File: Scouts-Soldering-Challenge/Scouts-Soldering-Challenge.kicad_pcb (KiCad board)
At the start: 2 copper layers, 76.2 x 94 mm, 14 parts, among them SW1 SW_Push

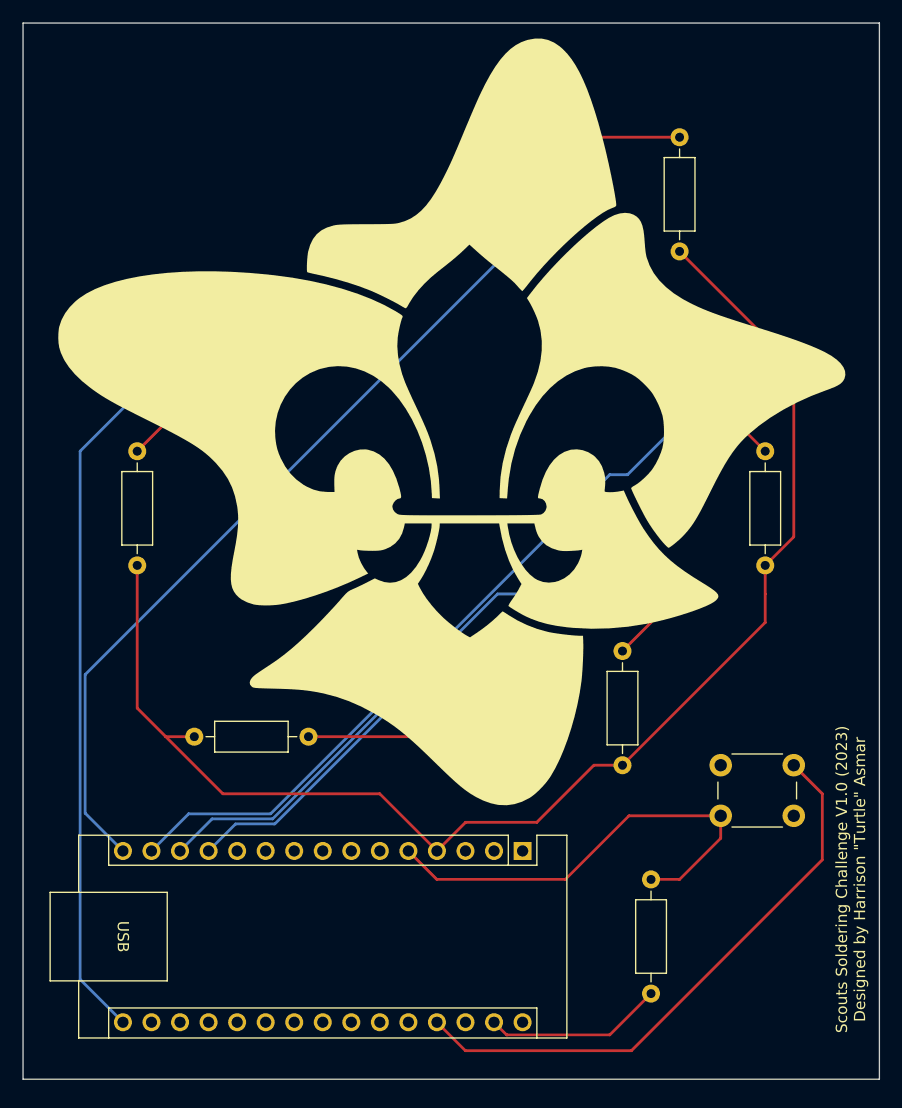
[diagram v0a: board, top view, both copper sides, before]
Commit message: Updated some trace routes
Minor changes, still functionally the same
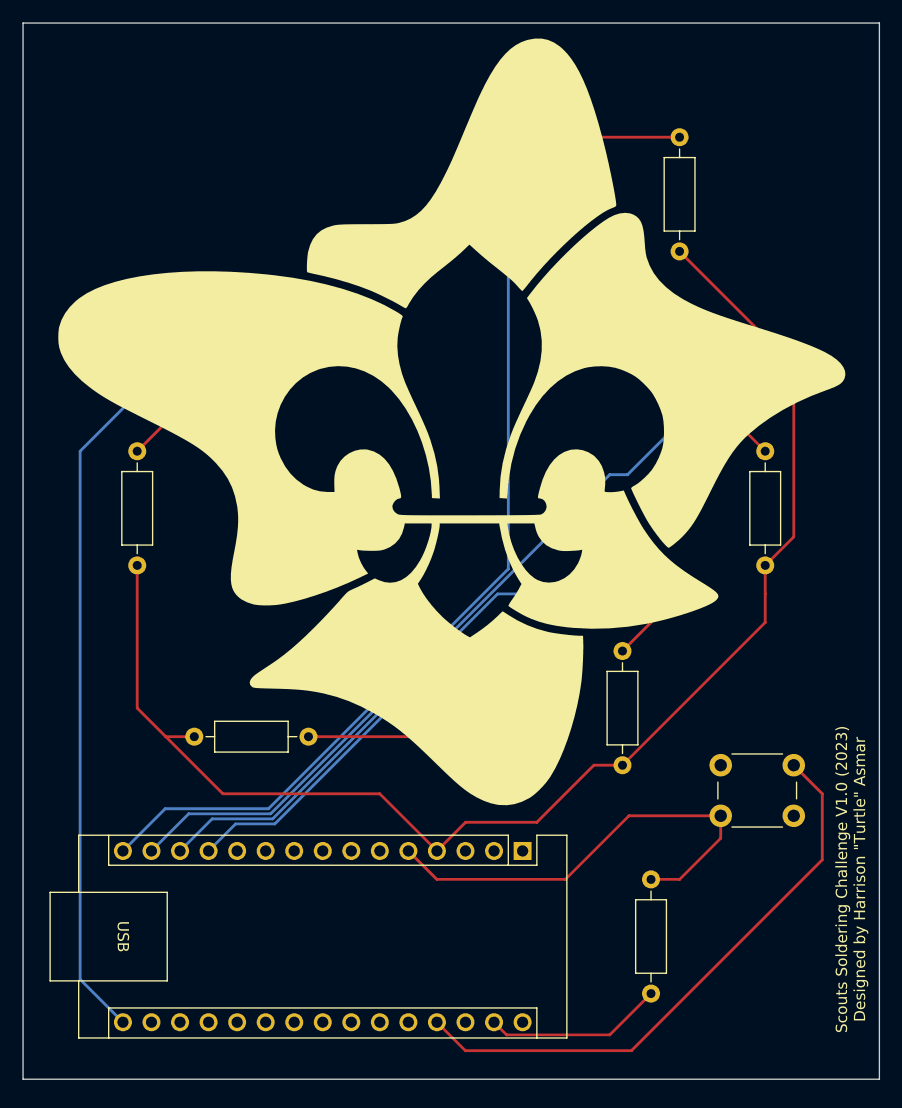
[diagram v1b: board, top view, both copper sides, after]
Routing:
- net Net-(A1-D12): track 80.5 -> 83.1 mm
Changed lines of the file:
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@@
   (segment (start 139.053198 119.075) (end 133.665 119.075) (width 0.25) (layer "B.Cu") (net 13))
   (segment (start 170.18 99.06) (end 159.068198 99.06) (width 0.25) (layer "B.Cu") (net 13))
+  (segment (start 177.8 81.28) (end 170.63 88.45) (width 0.25) (layer "B.Cu") (net 14))
+  (segment (start 169.041802 88.45) (end 138.866802 118.625) (width 0.25) (layer "B.Cu") (net 14))
+  (segment (start 131.575 118.625) (end 128.27 121.93) (width 0.25) (layer "B.Cu") (net 14))
+  (segment (start 177.8 78.74) (end 177.8 81.28) (width 0.25) (layer "B.Cu") (net 14))
   (segment (start 138.866802 118.625) (end 131.575 118.625) (width 0.25) (layer "B.Cu") (net 14))
-  (segment (start 177.8 78.74) (end 177.8 81.28) (width 0.25) (layer "B.Cu") (net 14))
-  (segment (start 169.041802 88.45) (end 138.866802 118.625) (width 0.25) (layer "B.Cu") (net 14))
-  (segment (start 177.8 81.28) (end 170.63 88.45) (width 0.25) (layer "B.Cu") (net 14))
-  (segment (start 131.575 118.625) (end 128.27 121.93) (width 0.25) (layer "B.Cu") (net 14))
   (segment (start 170.63 88.45) (end 169.041802 88.45) (width 0.25) (layer "B.Cu") (net 14))
-  (segment (start 160.02 68.58) (end 122.37 106.23) (width 0.25) (layer "B.Cu") (net 15))
-  (segment (start 160.02 58.42) (end 160.02 68.58) (width 0.25) (layer "B.Cu") (net 15))
-  (segment (start 122.37 106.23) (end 122.37 118.57) (width 0.25) (layer "B.Cu") (net 15))
-  (segment (start 122.37 118.57) (end 125.73 121.93) (width 0.25) (layer "B.Cu") (net 15))
-  (segment (start 121.92 133.36) (end 125.73 137.17) (width 0.25) (layer "B.Cu") (net 16))
-  (segment (start 121.92 86.36) (end 121.92 133.36) (width 0.25) (layer "B.Cu") (net 16))
+  (segment (start 138.680406 118.175) (end 129.485 118.175) (width 0.25) (layer "B.Cu") (net 15))
+  (segment (start 160.02 58.42) (end 160.02 96.835406) (width 0.25) (layer "B.Cu") (net 15))
+  (segment (start 160.02 96.835406) (end 138.680406 118.175) (width 0.25) (layer "B.Cu") (net 15))
+  (segment (start 129.485 118.175) (end 125.73 121.93) (width 0.25) (layer "B.Cu") (net 15))
   (segment (start 129.54 76.2) (end 129.54 78.74) (width 0.25) (layer "B.Cu") (net 16))
   (segment (start 129.54 78.74) (end 121.92 86.36) (width 0.25) (layer "B.Cu") (net 16))
+  (segment (start 121.92 86.36) (end 121.92 133.36) (width 0.25) (layer "B.Cu") (net 16))
+  (segment (start 121.92 133.36) (end 125.73 137.17) (width 0.25) (layer "B.Cu") (net 16))
   (segment (start 170.975496 139.7) (end 156.2 139.7) (width 0.25) (layer "F.Cu") (net 27))
   (segment (start 187.96 122.715496) (end 170.975496 139.7) (width 0.25) (layer "F.Cu") (net 27))

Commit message: Rotated LEDs to adapt to updated schematic
LEDs now have the correct leg connecting to the square ground pad. Old PCB design still works, but this is now in line with standard design principles.
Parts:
- D1: renamed from D1 YELLOW
- D2: renamed from D2 ORANGE
- D3: renamed from D3 MAROON
- D4: renamed from D4 GREEN
- D5: renamed from D5 RED
- R2: renamed from  330R
- R6: renamed from 330R; value 330R -> 10KR
- moved D2 2.54 mm to (160.0, 109.2), turned to 180 degrees
- moved D5 2.54 mm to (132.1, 76.2), turned to 180 degrees
- moved D1 2.54 mm to (162.6, 58.4), turned to 180 degrees
- moved D3 2.54 mm to (172.7, 99.1), turned to 180 degrees
- moved D4 2.54 mm to (180.3, 78.7), turned to 180 degrees
- renumbered 330R to R1, 330R to R3, 330R to R4, 330R to R5
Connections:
- D1 pad 1: Net-(A1-D12) -> Net-(D1-K)
- D1 pad 2: Net-(D1-A) -> Net-(A1-D12)
- D2 pad 1: Net-(A1-D9) -> Net-(D2-K)
- D2 pad 2: Net-(D2-A) -> Net-(A1-D9)
- D3 pad 1: Net-(A1-D10) -> Net-(D3-K)
- D3 pad 2: Net-(D3-A) -> Net-(A1-D10)
- D4 pad 1: Net-(A1-D11) -> Net-(D4-K)
- D4 pad 2: Net-(D4-A) -> Net-(A1-D11)
- D5 pad 1: Net-(A1-D13) -> Net-(D5-K)
- D5 pad 2: Net-(D5-A) -> Net-(A1-D13)
- R1 pad 1: Net-(D4-A) -> Net-(D4-K)
- R2 pad 1: Net-(D3-A) -> Net-(D3-K)
- R3 pad 1: Net-(D2-A) -> Net-(D2-K)
- R4 pad 1: Net-(D5-A) -> Net-(D5-K)
- R5 pad 1: Net-(D1-A) -> Net-(D1-K)
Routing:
- net Net-(D2-K): track 0.00 -> 20.3 mm
- net Net-(D2-A): track 20.3 -> 0.00 mm
- net Net-(D1-K): track 0.00 -> 12.7 mm
- net Net-(D1-A): track 12.7 -> 0.00 mm
- net Net-(D5-A): track 12.3 -> 0.00 mm
- net Net-(D4-K): track 0.00 -> 8.67 mm
- net Net-(D4-A): track 8.67 -> 0.00 mm
- net Net-(D5-K): track 0.00 -> 7.18 mm
- net Net-(D3-K): track 0.00 -> 6.13 mm
- net Net-(D3-A): track 6.13 -> 0.00 mm
- net Net-(A1-D13): track 65.7 -> 63.2 mm
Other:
- board text added: "10KR"
- board text added: "300R"
- board text added: "330R"
- board text added: "GREEN"
- board text added: "MAROON"
- board text added: "ORANGE"
- board text added: "RED"
- board text added: "YELLOW"

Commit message: Bumped PCB Version to V1.1
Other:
- board text added: "Scouts Soldering Challenge V1.1 (2023) Designed by Harrison {dblquote}Turtle{dblquote} Asmar"
- board text removed: "Scouts Soldering Challenge V1.0 (2023) Designed by Harrison {dblquote}Turtle{dblquote} Asmar"
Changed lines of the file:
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@@
     (effects (font (size 1.5 1.5) (thickness 0.3) bold) (justify left bottom mirror))
   )
-  (gr_text "Scouts Soldering Challenge V1.0 (2023)\nDesigned by Harrison {dblquote}Turtle{dblquote} Asmar" (at 190.5 124.46 90) (layer "F.SilkS")
+  (gr_text "Scouts Soldering Challenge V1.1 (2023)\nDesigned by Harrison {dblquote}Turtle{dblquote} Asmar" (at 190.5 124.46 90) (layer "F.SilkS")
     (effects (font (size 1 1) (thickness 0.15)))
   )

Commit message: Fixed mistake of disconnected component
In the process of correcting the schematic changes, I disconnected one of the LEDs and forgot to reconnect it. This has been rectified.
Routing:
- net Net-(D5-K): track 7.18 -> 12.3 mm
- net Net-(A1-D13): track 63.2 -> 65.7 mm
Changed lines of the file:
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@@
   (segment (start 160.02 96.835406) (end 138.680406 118.175) (width 0.25) (layer "B.Cu") (net 15))
   (segment (start 129.54 78.74) (end 121.92 86.36) (width 0.25) (layer "B.Cu") (net 16))
+  (segment (start 129.54 78.74) (end 129.54 76.2) (width 0.25) (layer "B.Cu") (net 16))
   (segment (start 121.92 86.36) (end 121.92 133.36) (width 0.25) (layer "B.Cu") (net 16))
   (segment (start 121.92 133.36) (end 125.73 137.17) (width 0.25) (layer "B.Cu") (net 16))
@@
   (segment (start 180.34 83.82) (end 182.88 86.36) (width 0.25) (layer "F.Cu") (net 34))
   (segment (start 132.08 81.28) (end 127 86.36) (width 0.25) (layer "F.Cu") (net 35))
+  (segment (start 132.08 81.28) (end 132.08 76.2) (width 0.25) (layer "F.Cu") (net 35))
 )
